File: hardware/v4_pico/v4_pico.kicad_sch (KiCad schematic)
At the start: 90 parts, among them J1 joystick, J2 LED strip, J3 SSD1306 SPI, J4 MIDI OUT Y:M5 - R:M4, J5 Batt, J6 Neck - Y:O BK:B R:3.3, J7 01x03, J8 MXP5010, Q1 2N7000, U1 74HC165, U2 74HC165, U3 74HC165

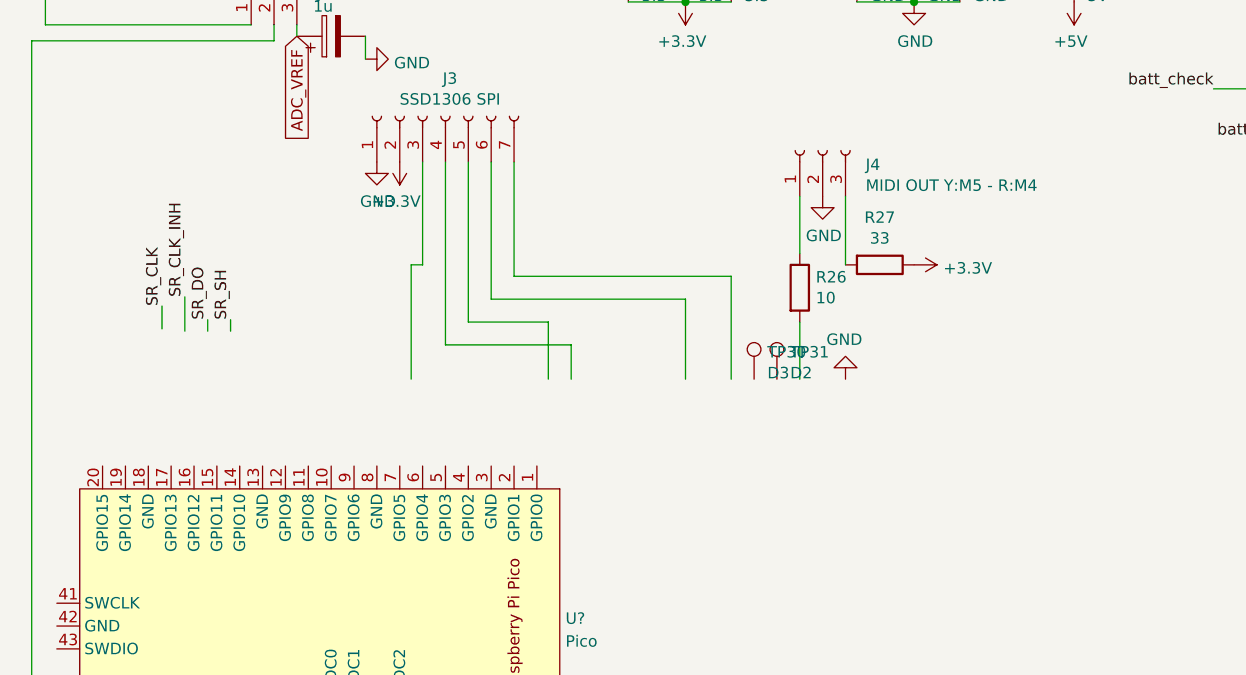
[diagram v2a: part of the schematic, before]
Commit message: Wired screen and shift register v4
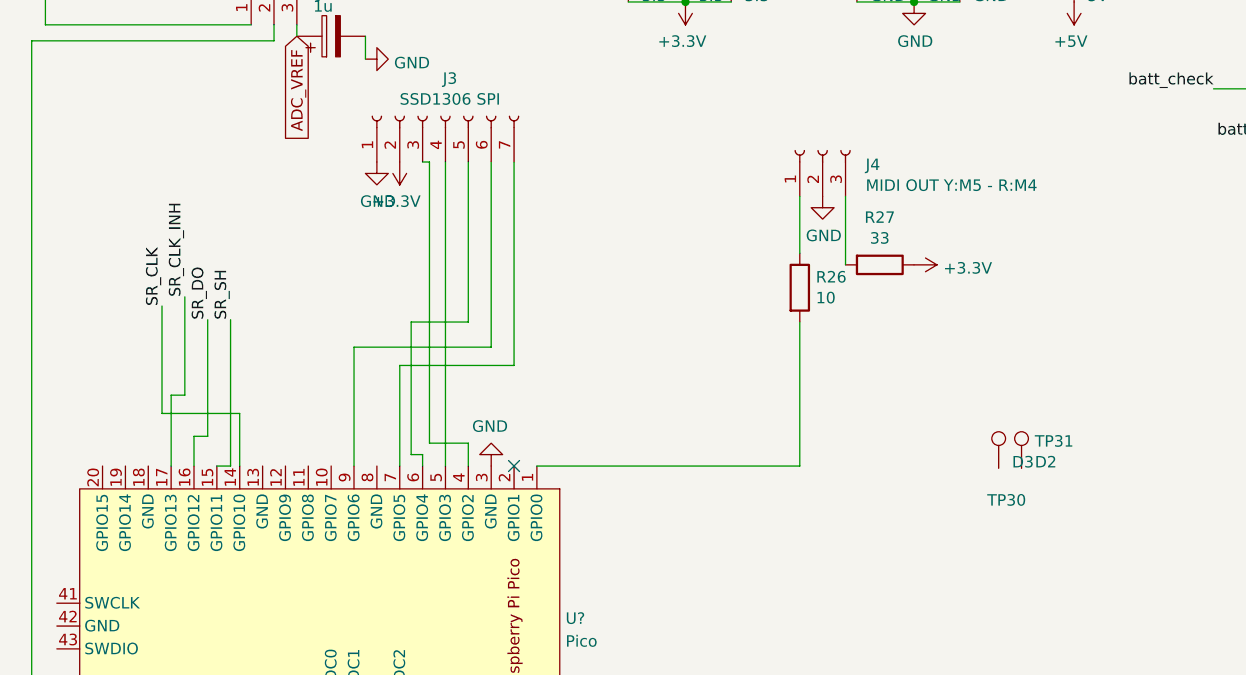
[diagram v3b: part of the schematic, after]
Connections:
- net GND: now also U?.3 (GND)
- net SR_CLK: now also U?.14 (GPIO10)
- net SR_CLK_INH: now also U?.17 (GPIO13)
- net SR_DO: now also U?.16 (GPIO12)
- net SR_SH: now also U?.15 (GPIO11)
- net at J3.3 (Pin_3): now also U?.4 (GPIO2)
- net at J3.4 (Pin_4): now also U?.5 (GPIO3)
- net at J3.5 (Pin_5): now also U?.6 (GPIO4)
- net at J3.6 (Pin_6): now also U?.9 (GPIO6)
- net at J3.7 (Pin_7): now also U?.7 (GPIO5)
- net at R26.2: now also U?.1 (GPIO0)
- no-connect marks 10 -> 11
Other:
- moved on the sheet: TP30, TP31

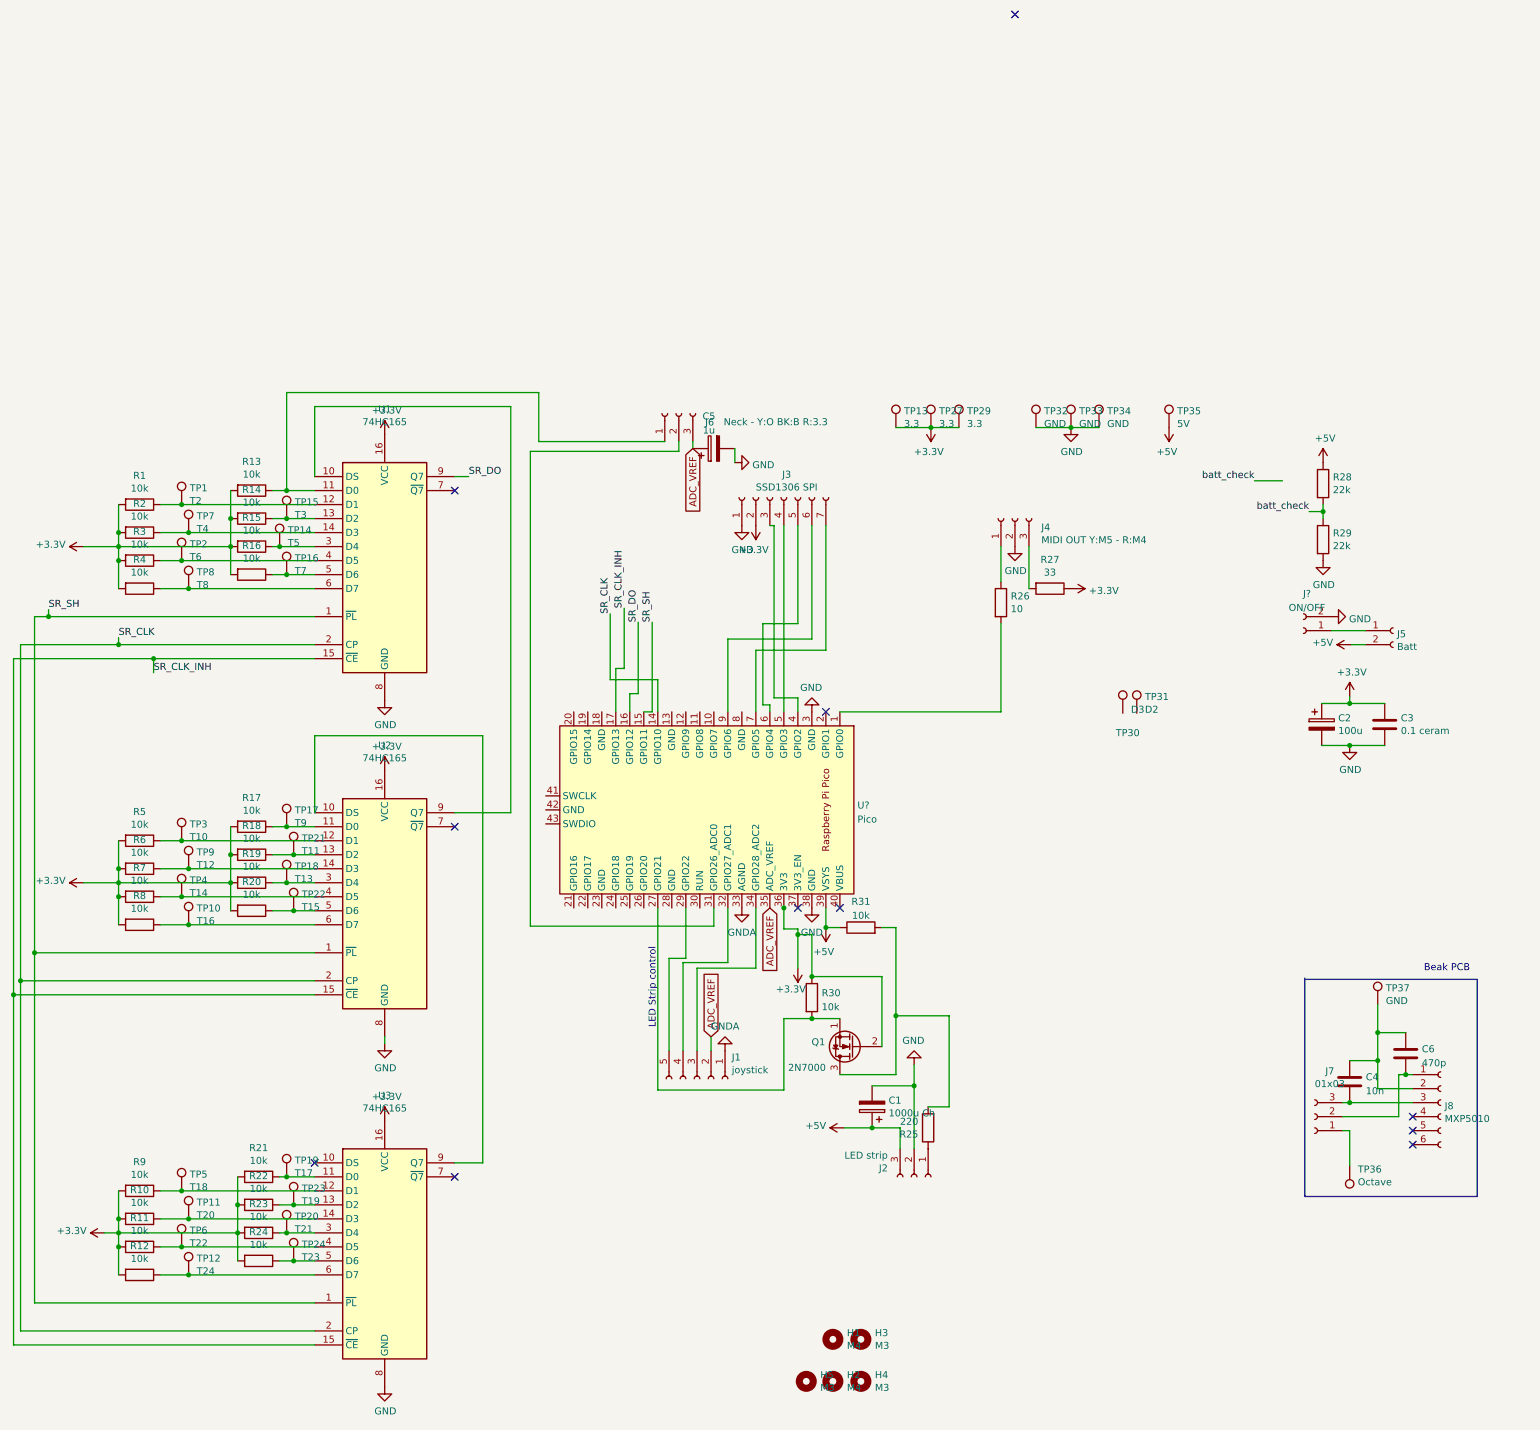
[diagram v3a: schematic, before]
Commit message: Added ADC component for battery check
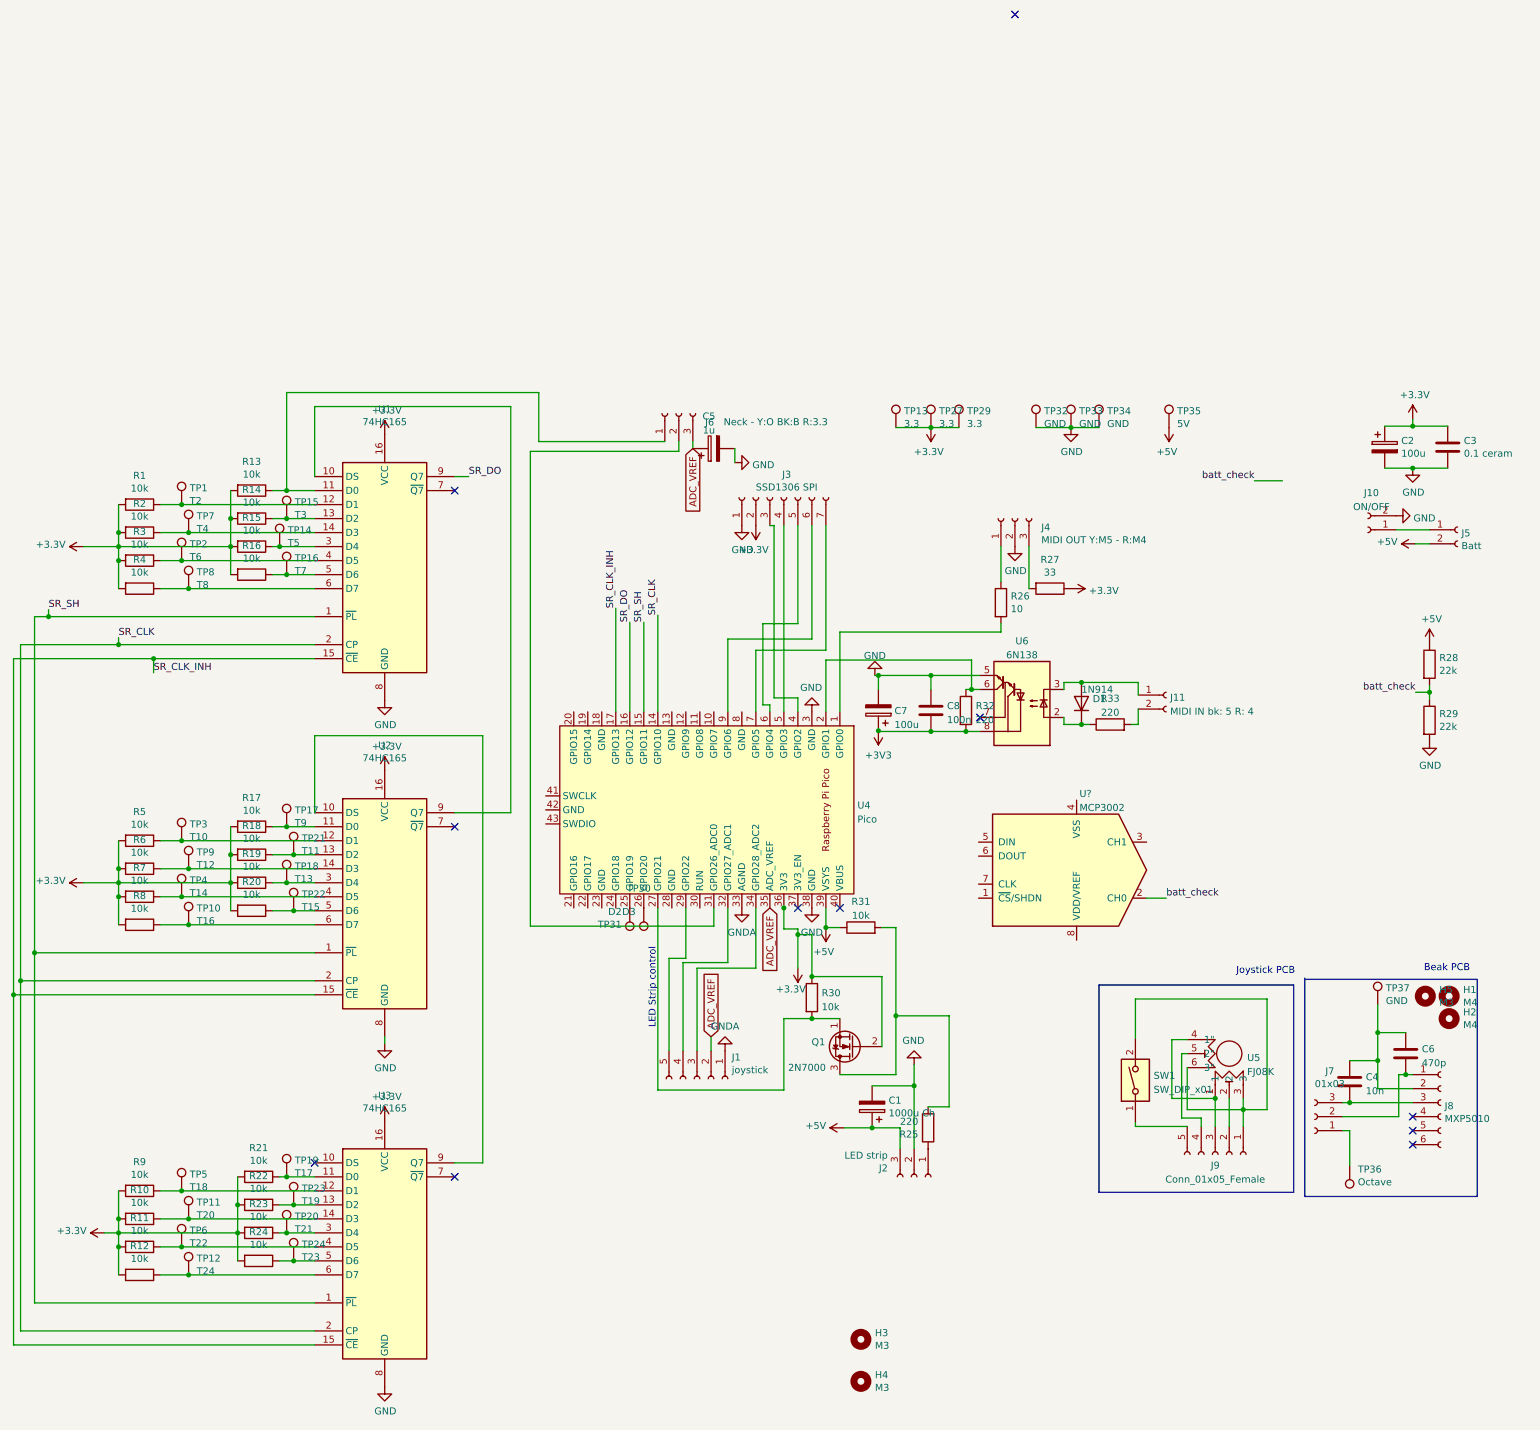
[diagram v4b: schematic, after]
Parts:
- added C7: 100u, Capacitor_THT:CP_Radial_D7.5mm_P2.50mm, symbol Device:C_Polarized
- added C8: 100n, Capacitor_THT:C_Axial_L3.8mm_D2.6mm_P7.50mm_Horizontal, symbol Device:C
- added D1: 1N914, Diode_THT:D_DO-34_SOD68_P7.62mm_Horizontal, symbol Device:D
- added J11: MIDI IN bk: 5 R: 4, symbol Connector:Conn_01x02_Female
- added J9: Conn_01x05_Female, symbol Connector:Conn_01x05_Female
- added R32, R33: 220, Resistor_THT:R_Axial_DIN0207_L6.3mm_D2.5mm_P7.62mm_Horizontal, symbol Device:R
- added SW1: SW_DIP_x01, symbol Switch:SW_DIP_x01
- added U5: FJ08K, symbol FJ08K_flat_joystick:FJ08K
- added U6: 6N138, Package_DIP:DIP-8_W7.62mm_Socket, symbol Isolator:6N138
- added U?: MCP3002, symbol Analog_ADC:MCP3002
- gave numbers to parts that had none: 2
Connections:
- net GND: now also C7.2, C8.1, U6.5 (GND)
- net batt_check: now also U?.2 (CH0)
- net at TP31.1: now also U4.25 (GPIO19)
- net at TP30.1: now also U4.26 (GPIO20)
- net at U4.2 (GPIO1): now also R32.1, U6.6 (VO2)
- new net: J9.5 (Pin_5), SW1.1
- new net: J9.1 (Pin_1), SW1.2, U5.3, U5.6 (3")
- new net: D1.1 (K), R33.1, U6.2 (C1)
- new net: D1.2 (A), J11.1 (Pin_1), U6.3 (C2)
- new net: C7.1, C8.2, R32.2, U6.8 (VCC)
- new net: J9.3 (Pin_3), U5.1, U5.4 (1")
- new net: J9.2 (Pin_2), U5.2
- new net: J9.4 (Pin_4), U5.5 (2")
- new net: J11.2 (Pin_2), R33.2
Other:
- note added: "Joystick PCB"
- moved on the sheet: C2, C3, H1, H2, H5, J10, J5, R28, R29, TP30, TP31

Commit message: Schematic and assign for saxo pico
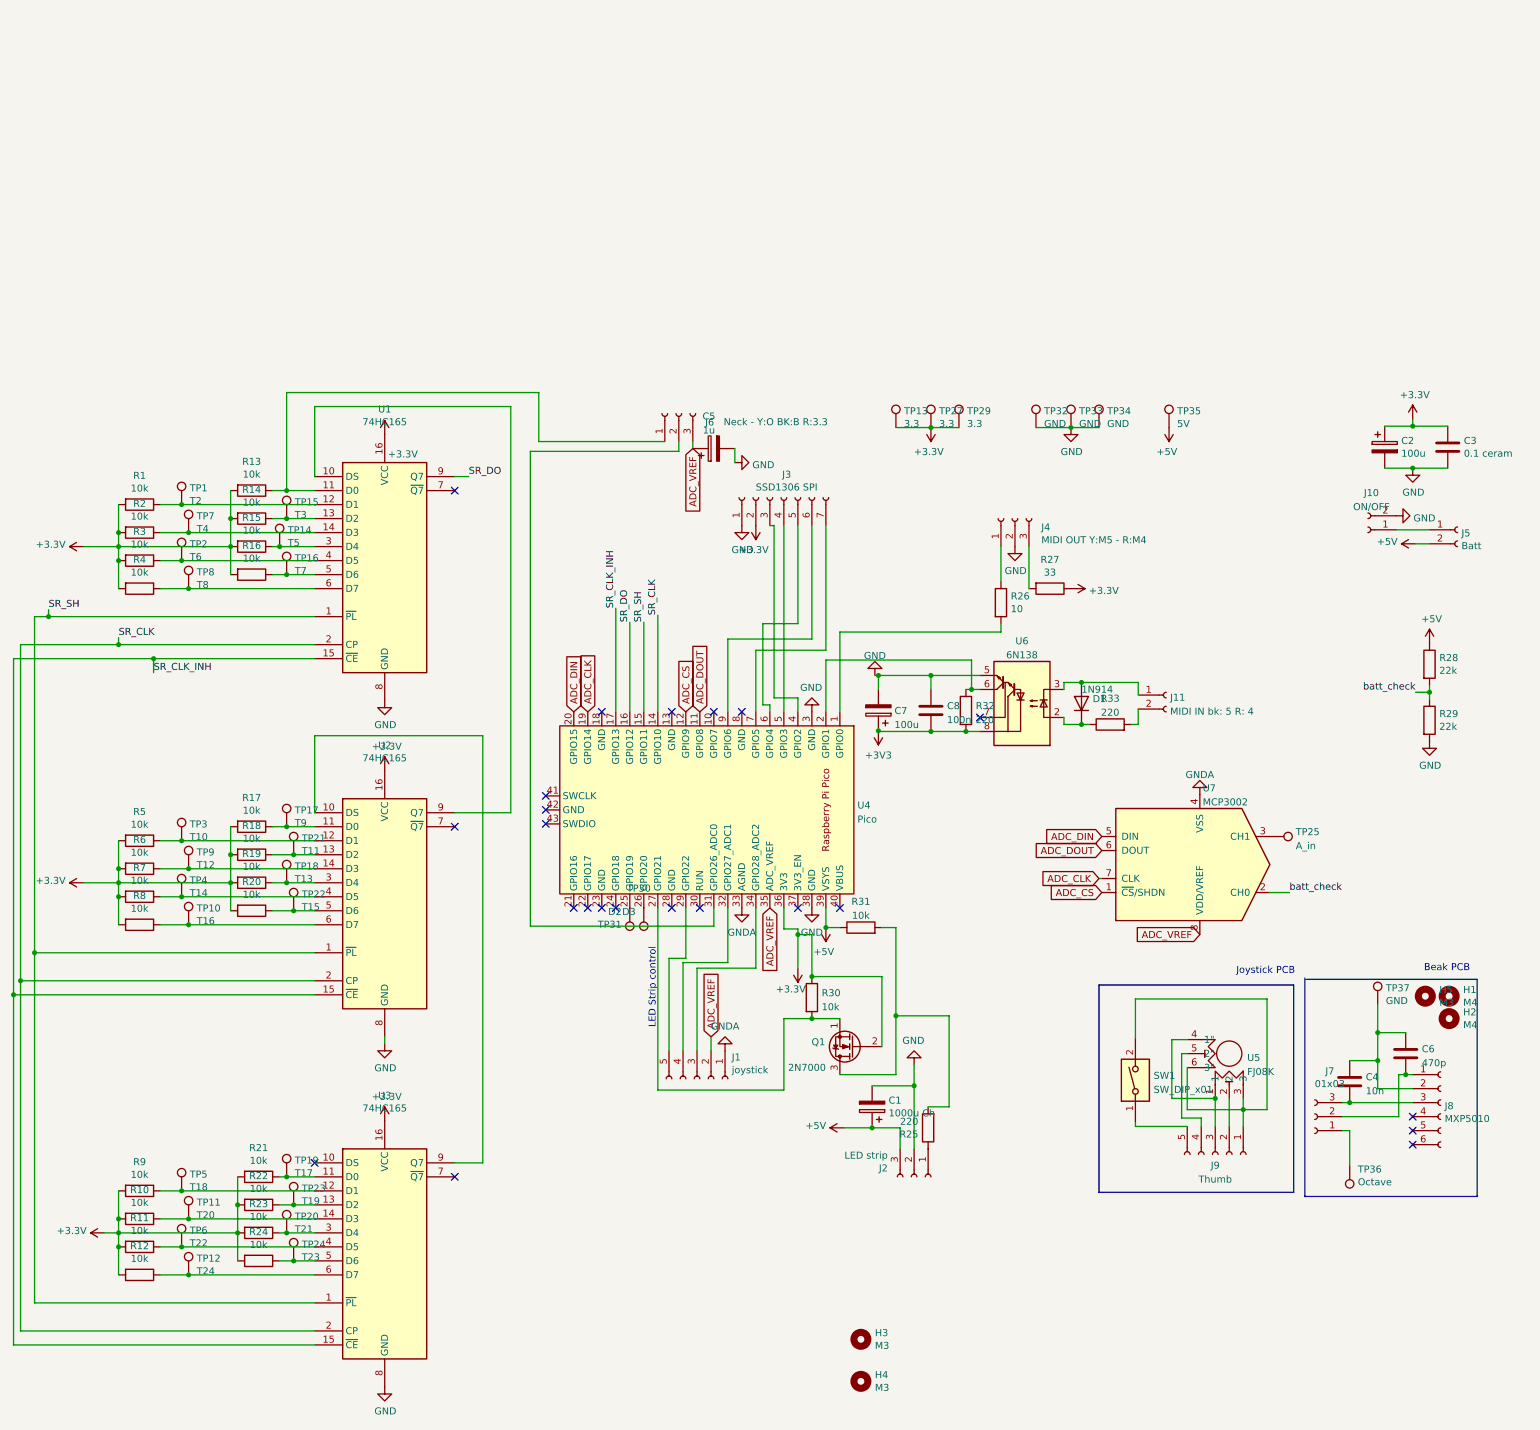
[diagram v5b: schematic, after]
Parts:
- added TP25: A_in, TestPoint:TestPoint_THTPad_2.5x2.5mm_Drill1.2mm, symbol Connector:TestPoint
- J10, J11: footprint (none) -> Connector_JST:JST_XH_B2B-XH-A_1x02_P2.50mm_Vertical
- J9: value Conn_01x05_Female -> Thumb; footprint (none) -> Connector_JST:JST_PH_B5B-PH-K_1x05_P2.00mm_Vertical
- R1, R10, R11, R12, R13, R14, R15, R16, R17, R18, R19, R2, R20, R21, R22, R23, R24, R3, R4, R5, R6, R7, R8, R9: footprint Resistor_THT:R_Axial_DIN0207_L6.3mm_D2.5mm_P7.62mm_Horizontal -> Resistor_SMD:R_1206_3216Metric_Pad1.30x1.75mm_HandSolder
- SW1: footprint (none) -> Multi_switch:Multi_switch
- U5: footprint (none) -> FJ08K:FJ08K
- U7: renamed from U?; footprint (none) -> Package_DIP:DIP-8_W7.62mm
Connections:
- net ADC_VREF: now also U7.8 (VDD/VREF)
- net GNDA: now also U7.4 (VSS)
- net ADC_DOUT: now reaches U4.11 (GPIO8)
- net ADC_DOUT: now also U7.6 (DOUT)
- net ADC_CS: now reaches U4.12 (GPIO9)
- net ADC_CS: now also U7.1 (~{CS}/SHDN)
- net ADC_CLK: now reaches U4.19 (GPIO14)
- net ADC_CLK: now also U7.7 (CLK)
- net ADC_DIN: now reaches U4.20 (GPIO15)
- net ADC_DIN: now also U7.5 (DIN)
- net at U7.3 (CH1): now also TP25.1
- no-connect marks 11 -> 23
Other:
- moved on the sheet: U7
